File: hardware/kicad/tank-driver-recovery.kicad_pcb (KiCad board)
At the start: 2 copper layers, 170 x 110 mm, 15 parts, among them P101 JTR-PRI, P102 JTR-SEC, P103 JTR-PWR, Q101 BD139-16, Q102 BD140-16, Q103 BD139-16, Q104 BD140-16, U101 OPA1656IDR, U102 OPA1656IDR, U103 OPA1656IDR, U104 OPA1656IDR

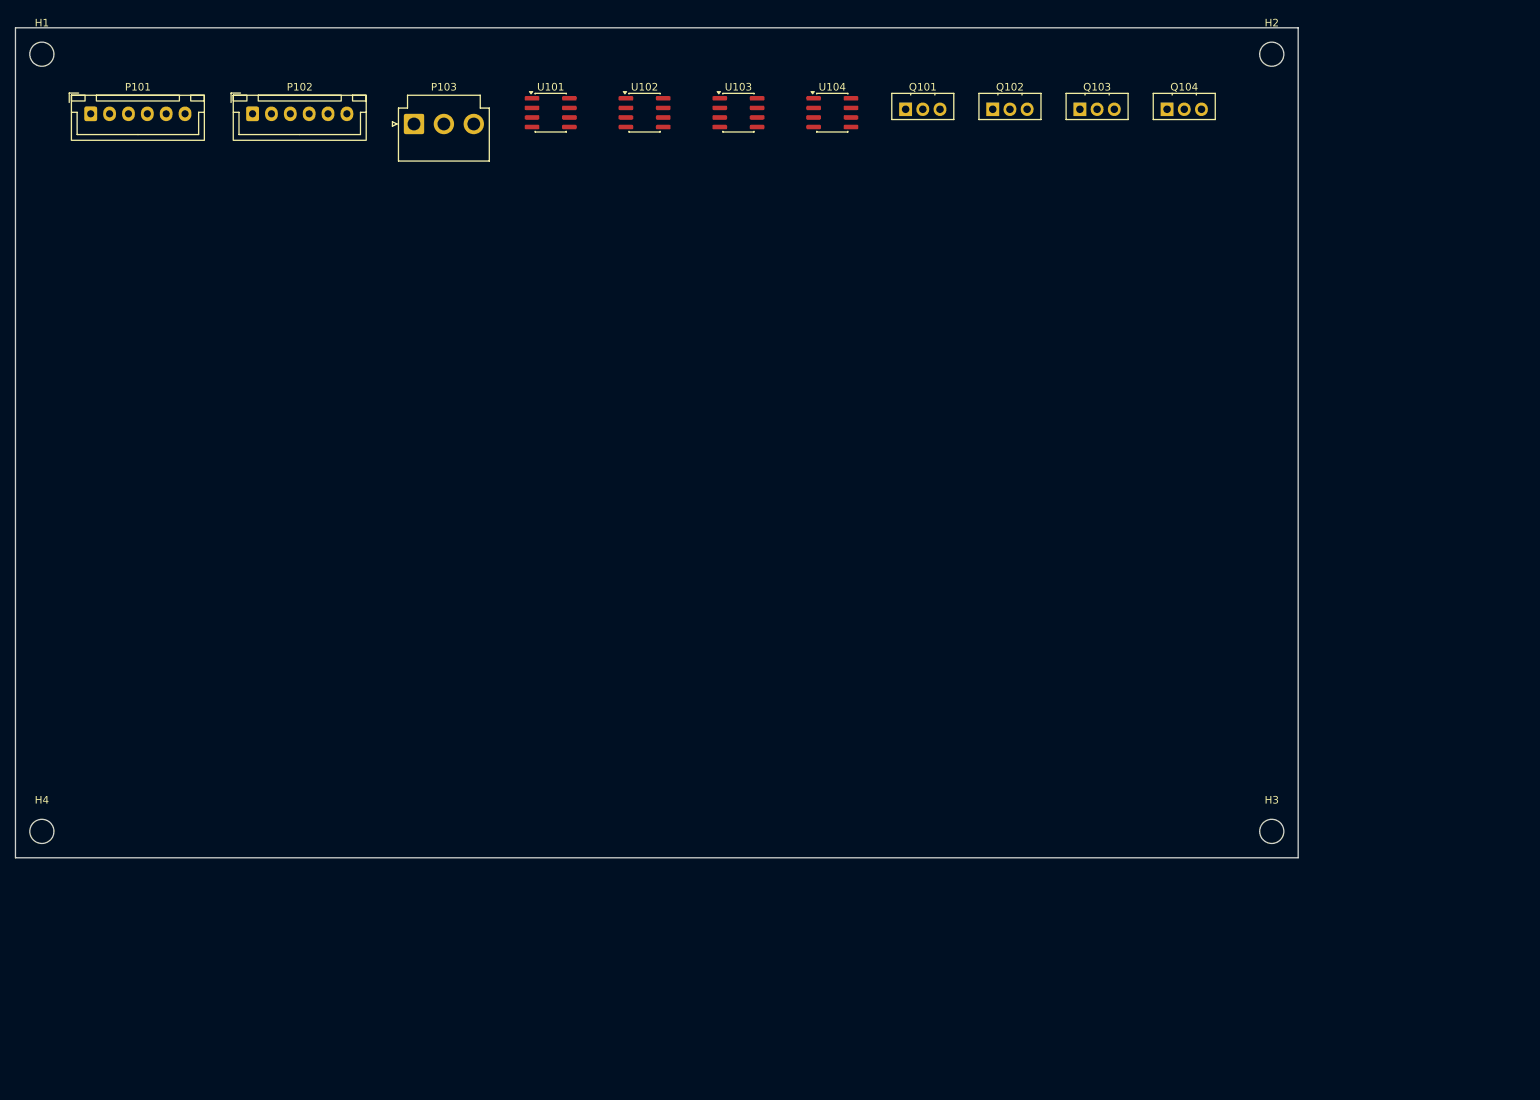
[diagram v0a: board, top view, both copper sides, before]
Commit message: Rebuild tank-driver-recovery: ERC-clean schematic + working ngspice testbench + netlist-synced placed PCB (DRC errors 0, routing pending)
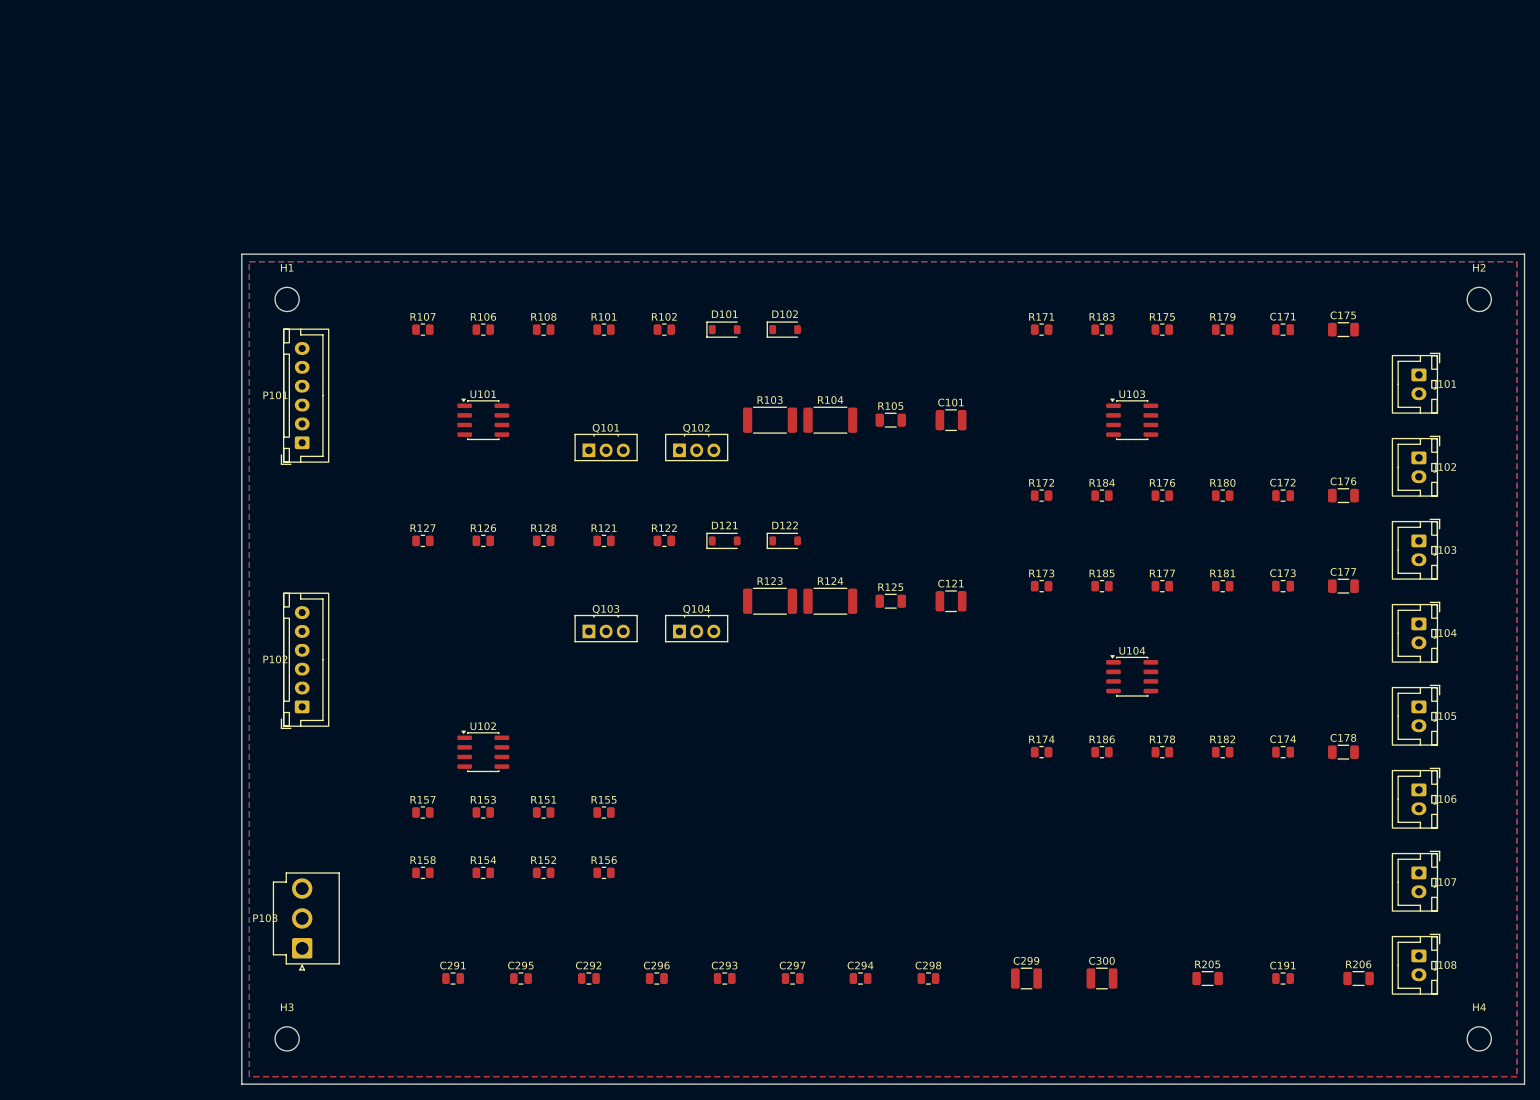
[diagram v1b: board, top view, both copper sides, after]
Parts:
- added C101: 47n, Capacitor_SMD:C_1210_3225Metric, F.Cu at (124.0, 52.0)
- added C121: 47n, Capacitor_SMD:C_1210_3225Metric, F.Cu at (124.0, 76.0)
- added C171: 68p, Capacitor_SMD:C_0805_2012Metric, F.Cu at (168.0, 40.0)
- added C172: 68p, Capacitor_SMD:C_0805_2012Metric, F.Cu at (168.0, 62.0)
- added C173: 68p, Capacitor_SMD:C_0805_2012Metric, F.Cu at (168.0, 74.0)
- added C174: 68p, Capacitor_SMD:C_0805_2012Metric, F.Cu at (168.0, 96.0)
- added C175: 22n, Capacitor_SMD:C_1206_3216Metric, F.Cu at (176.0, 40.0)
- added C176: 22n, Capacitor_SMD:C_1206_3216Metric, F.Cu at (176.0, 62.0)
- added C177: 22n, Capacitor_SMD:C_1206_3216Metric, F.Cu at (176.0, 74.0)
- added C178: 22n, Capacitor_SMD:C_1206_3216Metric, F.Cu at (176.0, 96.0)
- added C191: 1n, Capacitor_SMD:C_0805_2012Metric, F.Cu at (168.0, 126.0)
- added C291: 100n, Capacitor_SMD:C_0805_2012Metric, F.Cu at (58.0, 126.0)
- added C292: 100n, Capacitor_SMD:C_0805_2012Metric, F.Cu at (76.0, 126.0)
- added C293: 100n, Capacitor_SMD:C_0805_2012Metric, F.Cu at (94.0, 126.0)
- added C294: 100n, Capacitor_SMD:C_0805_2012Metric, F.Cu at (112.0, 126.0)
- added C295: 100n, Capacitor_SMD:C_0805_2012Metric, F.Cu at (67.0, 126.0)
- added C296: 100n, Capacitor_SMD:C_0805_2012Metric, F.Cu at (85.0, 126.0)
- added C297: 100n, Capacitor_SMD:C_0805_2012Metric, F.Cu at (103.0, 126.0)
- added C298: 100n, Capacitor_SMD:C_0805_2012Metric, F.Cu at (121.0, 126.0)
- added C299: 22u, Capacitor_SMD:C_1210_3225Metric, F.Cu at (134.0, 126.0)
- added C300: 22u, Capacitor_SMD:C_1210_3225Metric, F.Cu at (144.0, 126.0)
- added D101: 1N4148W, Diode_SMD:D_SOD-123, F.Cu at (94.0, 40.0)
- added D102: 1N4148W, Diode_SMD:D_SOD-123, F.Cu at (102.0, 40.0)
- added D121: 1N4148W, Diode_SMD:D_SOD-123, F.Cu at (94.0, 68.0)
- added D122: 1N4148W, Diode_SMD:D_SOD-123, F.Cu at (102.0, 68.0)
- added J101: PRI L SEND, Connector_JST:JST_XH_B2B-XH-A_1x02_P2.50mm_Vertical, F.Cu at (186.0, 46.0)
- added J102: PRI L RET, Connector_JST:JST_XH_B2B-XH-A_1x02_P2.50mm_Vertical, F.Cu at (186.0, 57.0)
- added J103: PRI R SEND, Connector_JST:JST_XH_B2B-XH-A_1x02_P2.50mm_Vertical, F.Cu at (186.0, 68.0)
- added J104: PRI R RET, Connector_JST:JST_XH_B2B-XH-A_1x02_P2.50mm_Vertical, F.Cu at (186.0, 79.0)
- added J105: SEC L SEND, Connector_JST:JST_XH_B2B-XH-A_1x02_P2.50mm_Vertical, F.Cu at (186.0, 90.0)
- added J106: SEC L RET, Connector_JST:JST_XH_B2B-XH-A_1x02_P2.50mm_Vertical, F.Cu at (186.0, 101.0)
- added J107: SEC R SEND, Connector_JST:JST_XH_B2B-XH-A_1x02_P2.50mm_Vertical, F.Cu at (186.0, 112.0)
- added J108: SEC R RET, Connector_JST:JST_XH_B2B-XH-A_1x02_P2.50mm_Vertical, F.Cu at (186.0, 123.0)
- added R101: 68, Resistor_SMD:R_0805_2012Metric, F.Cu at (78.0, 40.0)
- added R102: 68, Resistor_SMD:R_0805_2012Metric, F.Cu at (86.0, 40.0)
- added R103: 0.33, Resistor_SMD:R_2512_6332Metric, F.Cu at (100.0, 52.0)
- added R104: 0.33, Resistor_SMD:R_2512_6332Metric, F.Cu at (108.0, 52.0)
- added R105: 10, Resistor_SMD:R_1206_3216Metric, F.Cu at (116.0, 52.0)
- added R106: 1k, Resistor_SMD:R_0805_2012Metric, F.Cu at (62.0, 40.0)
- added R107: 10k, Resistor_SMD:R_0805_2012Metric, F.Cu at (54.0, 40.0)
- added R108: 10k, Resistor_SMD:R_0805_2012Metric, F.Cu at (70.0, 40.0)
- added R121: 68, Resistor_SMD:R_0805_2012Metric, F.Cu at (78.0, 68.0)
- added R122: 68, Resistor_SMD:R_0805_2012Metric, F.Cu at (86.0, 68.0)
- added R123: 0.33, Resistor_SMD:R_2512_6332Metric, F.Cu at (100.0, 76.0)
- added R124: 0.33, Resistor_SMD:R_2512_6332Metric, F.Cu at (108.0, 76.0)
- added R125: 10, Resistor_SMD:R_1206_3216Metric, F.Cu at (116.0, 76.0)
- added R126: 1k, Resistor_SMD:R_0805_2012Metric, F.Cu at (62.0, 68.0)
- added R127: 10k, Resistor_SMD:R_0805_2012Metric, F.Cu at (54.0, 68.0)
- added R128: 10k, Resistor_SMD:R_0805_2012Metric, F.Cu at (70.0, 68.0)
- added R151: 12k, Resistor_SMD:R_0805_2012Metric, F.Cu at (70.0, 104.0)
- added R152: 12k, Resistor_SMD:R_0805_2012Metric, F.Cu at (70.0, 112.0)
- added R153: 10k, Resistor_SMD:R_0805_2012Metric, F.Cu at (62.0, 104.0)
- added R154: 10k, Resistor_SMD:R_0805_2012Metric, F.Cu at (62.0, 112.0)
- added R155: 220, Resistor_SMD:R_0805_2012Metric, F.Cu at (78.0, 104.0)
- added R156: 220, Resistor_SMD:R_0805_2012Metric, F.Cu at (78.0, 112.0)
- added R157: 10k, Resistor_SMD:R_0805_2012Metric, F.Cu at (54.0, 104.0)
- added R158: 10k, Resistor_SMD:R_0805_2012Metric, F.Cu at (54.0, 112.0)
- added R171: 2.2Meg, Resistor_SMD:R_0805_2012Metric, F.Cu at (136.0, 40.0)
- added R172: 2.2Meg, Resistor_SMD:R_0805_2012Metric, F.Cu at (136.0, 62.0)
- added R173: 2.2Meg, Resistor_SMD:R_0805_2012Metric, F.Cu at (136.0, 74.0)
- added R174: 2.2Meg, Resistor_SMD:R_0805_2012Metric, F.Cu at (136.0, 96.0)
- added R175: 1k, Resistor_SMD:R_0805_2012Metric, F.Cu at (152.0, 40.0)
- added R176: 1k, Resistor_SMD:R_0805_2012Metric, F.Cu at (152.0, 62.0)
- added R177: 1k, Resistor_SMD:R_0805_2012Metric, F.Cu at (152.0, 74.0)
- added R178: 1k, Resistor_SMD:R_0805_2012Metric, F.Cu at (152.0, 96.0)
- added R179: 33k, Resistor_SMD:R_0805_2012Metric, F.Cu at (160.0, 40.0)
- added R180: 33k, Resistor_SMD:R_0805_2012Metric, F.Cu at (160.0, 62.0)
- added R181: 33k, Resistor_SMD:R_0805_2012Metric, F.Cu at (160.0, 74.0)
- added R182: 33k, Resistor_SMD:R_0805_2012Metric, F.Cu at (160.0, 96.0)
- added R183: 0, Resistor_SMD:R_0805_2012Metric, F.Cu at (144.0, 40.0)
- added R184: 0, Resistor_SMD:R_0805_2012Metric, F.Cu at (144.0, 62.0)
- added R185: 0, Resistor_SMD:R_0805_2012Metric, F.Cu at (144.0, 74.0)
- added R186: 0, Resistor_SMD:R_0805_2012Metric, F.Cu at (144.0, 96.0)
- added R205: 100, Resistor_SMD:R_1206_3216Metric, F.Cu at (158.0, 126.0)
- added R206: 0, Resistor_SMD:R_1206_3216Metric, F.Cu at (178.0, 126.0)
- H1, H2, H3, H4: value M3 NPTH -> M3; footprint MountingHole_3.2mm_M3 -> MountingHole:MountingHole_3.2mm_M3
- P101: value JTR-PRI -> JTR-PRI B6B-XH-A; footprint JST_XH_B6B-XH-A_1x06_P2.50mm_Vertical -> Connector_JST:JST_XH_B6B-XH-A_1x06_P2.50mm_Vertical
- P102: value JTR-SEC -> JTR-SEC B6B-XH-A; footprint JST_XH_B6B-XH-A_1x06_P2.50mm_Vertical -> Connector_JST:JST_XH_B6B-XH-A_1x06_P2.50mm_Vertical
- P103: value JTR-PWR -> JTR-PWR B3P-VH-B; footprint JST_VH_B3P-VH_1x03_P3.96mm_Vertical -> Connector_JST:JST_VH_B3P-VH_1x03_P3.96mm_Vertical
- Q101, Q102, Q103, Q104: footprint TO-126-3_Vertical -> Package_TO_SOT_THT:TO-126-3_Vertical
- U101, U102, U103, U104: footprint SOIC-8_3.9x4.9mm_P1.27mm -> Package_SO:SOIC-8_3.9x4.9mm_P1.27mm
- moved H4 192.5 mm to (194.0, 134.0)
- moved H3 133.4 mm to (36.0, 134.0)
- moved P103 110.3 mm to (38.0, 122.0), turned to 90 degrees
- moved Q103 95.0 mm to (76.0, 80.0)
- moved Q104 94.7 mm to (88.0, 80.0)
- moved U102 87.4 mm to (62.0, 96.0)
- moved U104 84.7 mm to (148.0, 86.0)
- moved P102 78.9 mm to (38.0, 90.0), turned to 90 degrees
- moved U103 66.2 mm to (148.0, 52.0)
- moved Q101 61.7 mm to (76.0, 56.0)
- moved Q102 61.4 mm to (88.0, 56.0)
- moved P101 51.8 mm to (38.0, 55.0), turned to 90 degrees
- moved H1 46.0 mm to (36.0, 36.0)
- moved H2 42.6 mm to (194.0, 36.0)
- moved U101 41.7 mm to (62.0, 52.0)
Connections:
- P101 pad 1: (no net) -> PRI_SEND_L
- P101 pad 2: (no net) -> PRI_RET_L
- P101 pad 3: (no net) -> AGND
- P101 pad 4: (no net) -> PRI_SEND_R
- P101 pad 5: (no net) -> PRI_RET_R
- P101 pad 6: (no net) -> AGND
- P102 pad 1: (no net) -> SEC_SEND_L
- P102 pad 2: (no net) -> SEC_RET_L
- P102 pad 3: (no net) -> AGND
- P102 pad 4: (no net) -> SEC_SEND_R
- P102 pad 5: (no net) -> SEC_RET_R
- P102 pad 6: (no net) -> AGND
- P103 pad 1: (no net) -> +15VA
- P103 pad 2: (no net) -> AGND
- P103 pad 3: (no net) -> -15VA
- Q101 pad 1: (no net) -> N_Q101_E
- Q101 pad 2: (no net) -> +15VA
- Q101 pad 3: (no net) -> N_Q101_B
- Q102 pad 1: (no net) -> N_Q102_E
- Q102 pad 2: (no net) -> -15VA
- Q102 pad 3: (no net) -> N_Q102_B
- Q103 pad 1: (no net) -> N_Q103_E
- Q103 pad 2: (no net) -> +15VA
- Q103 pad 3: (no net) -> N_Q103_B
- Q104 pad 1: (no net) -> N_Q104_E
- Q104 pad 2: (no net) -> -15VA
- Q104 pad 3: (no net) -> N_Q104_B
- U101 pad 1: (no net) -> PRI_DRV_L
- U101 pad 2: (no net) -> N_PRI_L_M
- U101 pad 3: (no net) -> N_PRI_L_P
- U101 pad 4: (no net) -> -15VA
- U101 pad 5: (no net) -> N_PRI_R_P
- U101 pad 6: (no net) -> N_PRI_R_M
- U101 pad 7: (no net) -> PRI_DRV_R
- U101 pad 8: (no net) -> +15VA
- U102 pad 1: (no net) -> SEC_DRV_L
- U102 pad 2: (no net) -> N_SEC_L_M
- U102 pad 3: (no net) -> N_SEC_L_P
- U102 pad 4: (no net) -> -15VA
- U102 pad 5: (no net) -> N_SEC_R_P
- U102 pad 6: (no net) -> N_SEC_R_M
- U102 pad 7: (no net) -> SEC_DRV_R
- U102 pad 8: (no net) -> +15VA
- U103 pad 1: (no net) -> PRI_RET_L
- U103 pad 2: (no net) -> N_PRI_RET_L_M
- U103 pad 3: (no net) -> N_REC_PL_IN
- U103 pad 4: (no net) -> -15VA
- U103 pad 5: (no net) -> N_REC_PR_IN
- U103 pad 6: (no net) -> N_PRI_RET_R_M
- U103 pad 7: (no net) -> PRI_RET_R
- U103 pad 8: (no net) -> +15VA
- U104 pad 1: (no net) -> SEC_RET_L
- U104 pad 2: (no net) -> N_SEC_RET_L_M
- U104 pad 3: (no net) -> N_REC_SL_IN
- U104 pad 4: (no net) -> -15VA
- U104 pad 5: (no net) -> N_REC_SR_IN
- U104 pad 6: (no net) -> N_SEC_RET_R_M
- U104 pad 7: (no net) -> SEC_RET_R
- U104 pad 8: (no net) -> +15VA
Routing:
- added copper zone on B.Cu, net AGND
- added copper zone on F.Cu, net AGND
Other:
- board text removed: "GAS Rev A - Tank Driver / Recovery Board"
- board text removed: "OUTLINE SCAFFOLD - NOT FOR FAB"

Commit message: Board 1 routed: 0 DRC errors, 0 unconnected; Freerouting pipeline; fab outputs (gerbers, drill, pos, BOM)
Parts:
- moved R205 71.2 mm to (193.0, 64.0), turned to 90 degrees
- moved C191 56.8 mm to (193.0, 75.0), turned to 90 degrees
- moved R206 42.7 mm to (193.0, 86.0), turned to 90 degrees
- moved C300 22.0 mm to (166.0, 126.0)
- moved C298 21.0 mm to (142.0, 126.0)
- moved C299 20.0 mm to (154.0, 126.0)
- moved C294 18.0 mm to (130.0, 126.0)
- moved C297 15.0 mm to (118.0, 126.0)
- moved C293 12.0 mm to (106.0, 126.0)
- moved C296 9.00 mm to (94.0, 126.0)
- moved C292 6.00 mm to (82.0, 126.0)
- moved C295 3.00 mm to (70.0, 126.0)
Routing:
- net +15VA: track 0.00 -> 389.1 mm, vias 0 -> 1
- net -15VA: track 0.00 -> 352.8 mm, vias 0 -> 4
- net PRI_RET_R: track 0.00 -> 159.3 mm, vias 0 -> 1
- net PRI_RET_L: track 0.00 -> 153.5 mm, vias 0 -> 3
- net SEC_RET_L: track 0.00 -> 145.2 mm, vias 0 -> 2
- net SEC_RET_R: track 0.00 -> 138.0 mm
- net PRI_OUT_L: track 0.00 -> 138.0 mm
- net PRI_OUT_R: track 0.00 -> 125.7 mm
- net SEC_OUT_L: track 0.00 -> 112.9 mm
- net SEC_OUT_R: track 0.00 -> 107.1 mm
- net TANK_SHIELD_RET: track 0.00 -> 89.5 mm
- net TANK_SHIELD_SEND: track 0.00 -> 88.0 mm, vias 0 -> 1
- net SEC_REC_R_IN: track 0.00 -> 83.0 mm, vias 0 -> 1
- net N_SEC_L_M: track 0.00 -> 80.1 mm, vias 0 -> 2
- net PRI_REC_R_IN: track 0.00 -> 74.8 mm
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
